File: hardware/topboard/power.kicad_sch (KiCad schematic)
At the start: 34 parts

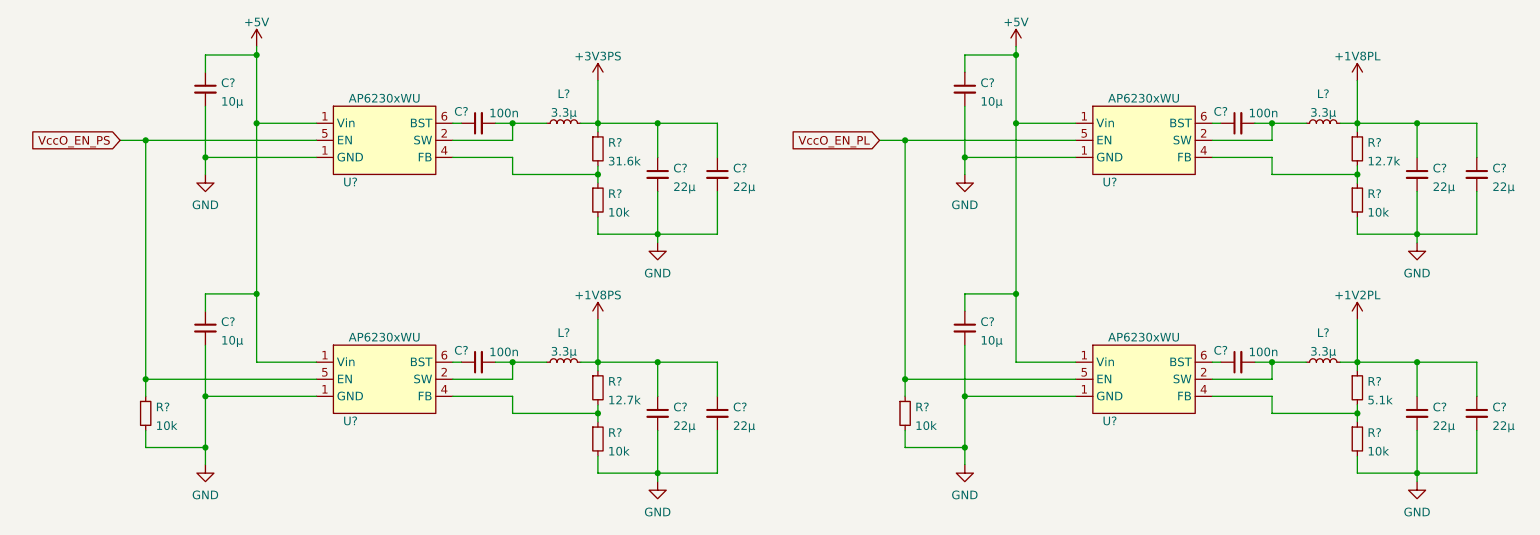
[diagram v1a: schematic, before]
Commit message: Fixing various top board issues
Signed-off-by: gatecat <gatecat@ds0.me>
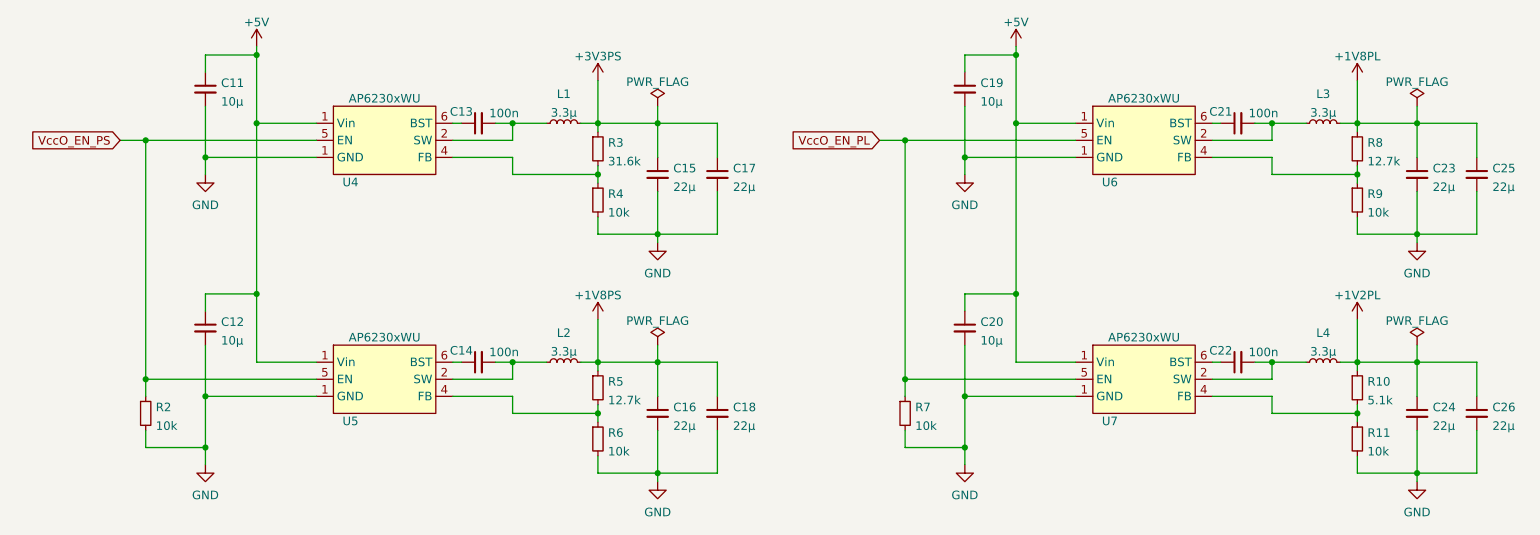
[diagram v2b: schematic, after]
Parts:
- gave numbers to parts that had none: 34

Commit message: Assign most top-board footprints
Signed-off-by: gatecat <gatecat@ds0.me>
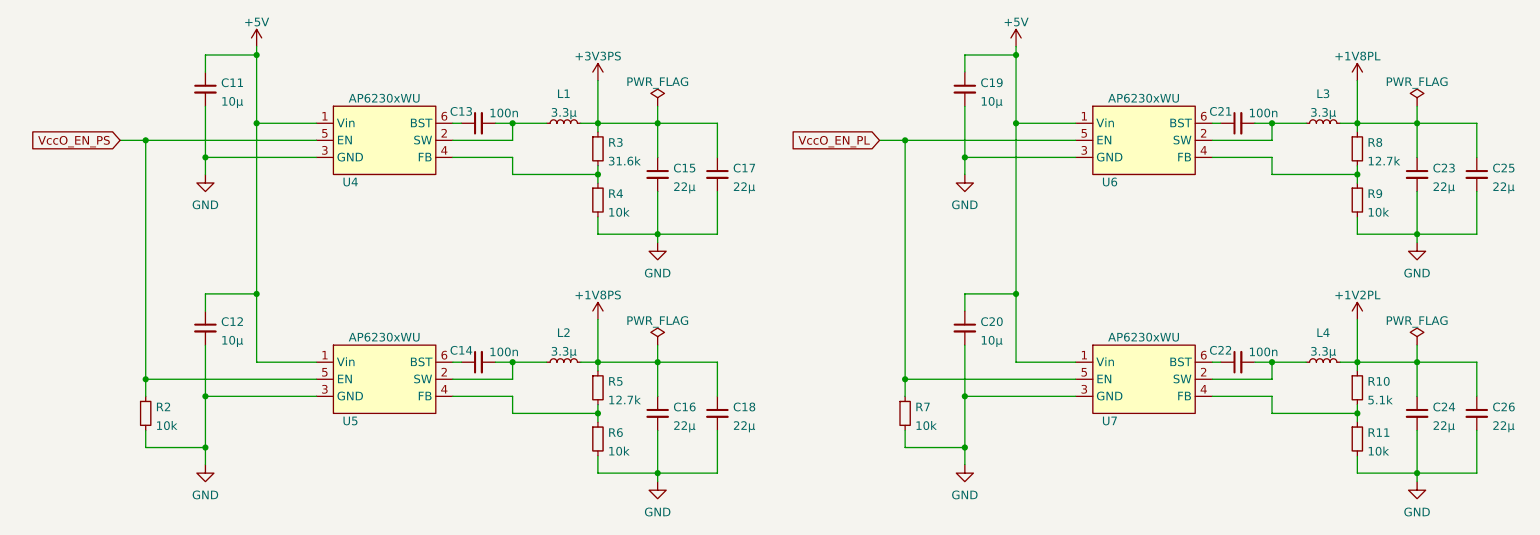
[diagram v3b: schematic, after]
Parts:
- C11, C12, C19, C20: footprint (none) -> Capacitor_SMD:C_0805_2012Metric
- C13, C14, C21, C22: footprint (none) -> Capacitor_SMD:C_0402_1005Metric
- C15, C16, C17, C18, C23, C24, C25, C26: footprint (none) -> Capacitor_SMD:C_1206_3216Metric
- L1, L2, L3, L4: footprint (none) -> meowality:BWVS00606045
- R10, R11, R2, R3, R4, R5, R6, R7, R8, R9: footprint (none) -> Resistor_SMD:R_0402_1005Metric
- U4, U5, U6, U7: footprint (none) -> Package_TO_SOT_SMD:TSOT-23-6
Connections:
- net GND: now also U4.3 (GND), U5.3 (GND), U6.3 (GND), U7.3 (GND); no longer U4.1 (Vin), U5.1 (Vin), U6.1 (Vin), U7.1 (Vin)
